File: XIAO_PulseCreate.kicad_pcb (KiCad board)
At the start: 2 copper layers, 72 x 48 mm, 19 parts, among them J1 MA735, J2 I2C OLED 0.91', J3 Power/Solenoid, J4 Trigger_IN, J5 Trigger_Out, Q1 2SK2232, SW1 MODE, SW2 +, SW3 -, U1 XIAO-RP2040-DIP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

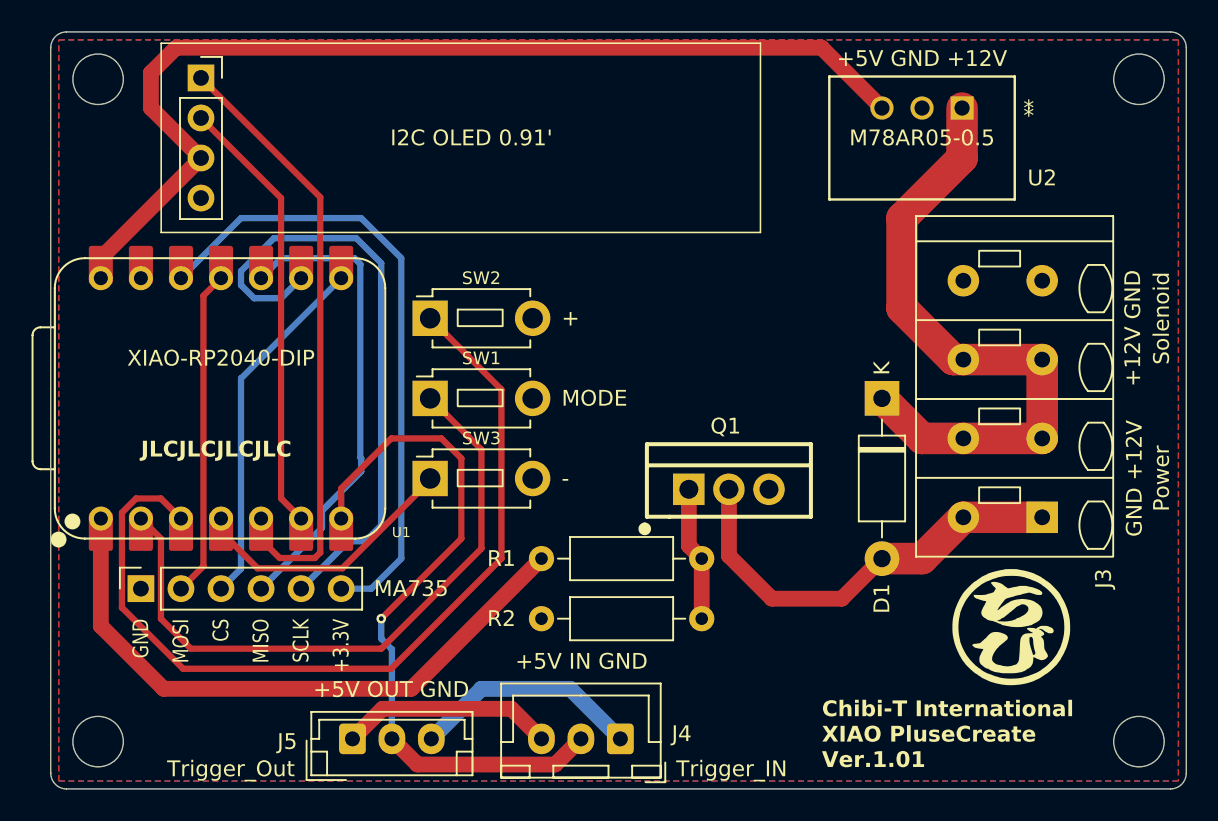
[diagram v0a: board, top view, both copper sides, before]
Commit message: Trigger_INの分圧抵抗を追加。 基板のソレノイドと電源の表記が逆だったので修正
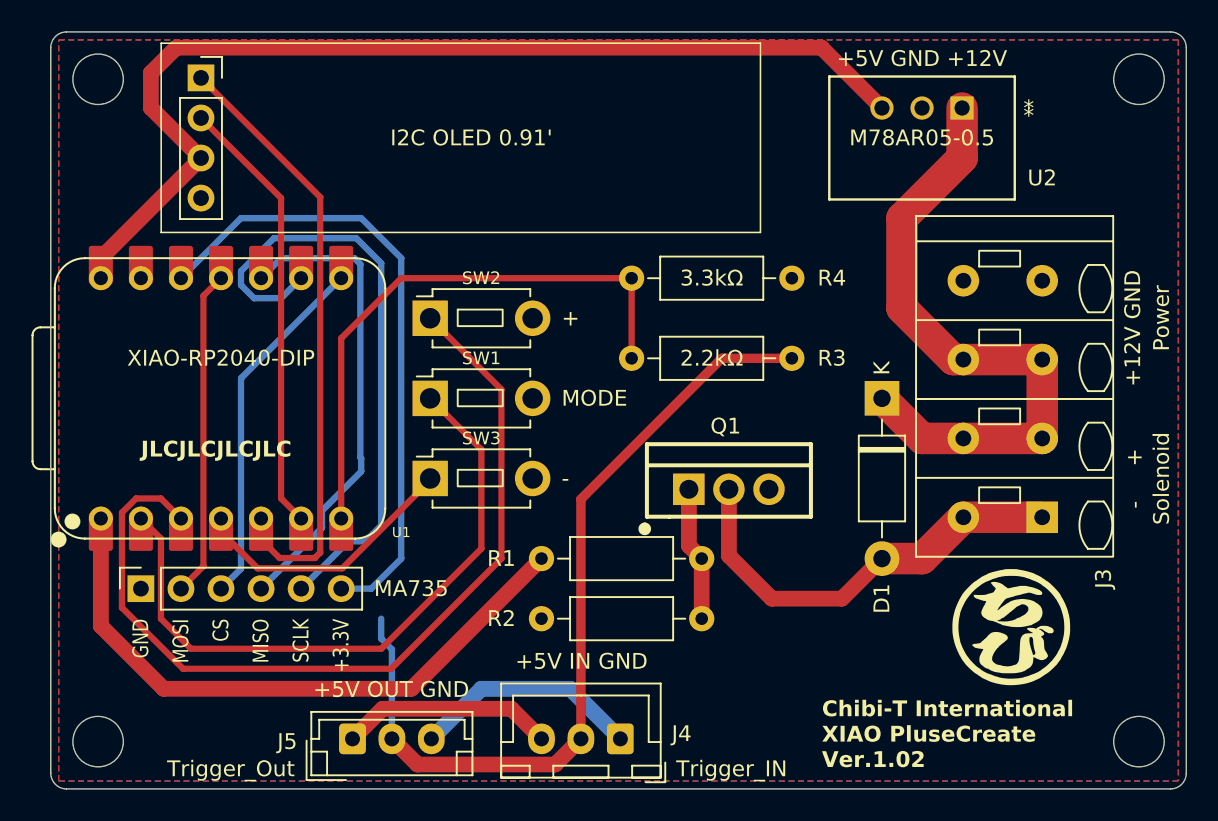
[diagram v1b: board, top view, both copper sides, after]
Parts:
- added R3: 2.2kΩ, Resistor_THT:R_Axial_DIN0207_L6.3mm_D2.5mm_P10.16mm_Horizontal, F.Cu at (177.0, 102.7)
- added R4: 3.3kΩ, Resistor_THT:R_Axial_DIN0207_L6.3mm_D2.5mm_P10.16mm_Horizontal, F.Cu at (177.0, 97.6)
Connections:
- net Net-(D1-A) renamed /-
- J4 pad 2: Trigger_IN -> Net-(J4-Pin_2)
- J5 pad 2: Trigger_IN -> Net-(J4-Pin_2)
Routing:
- net Net-(J4-Pin_2): track 0.00 -> 53.5 mm
- net Trigger_IN: track 44.9 -> 36.5 mm, vias 1 -> 0
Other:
- board text added: "- +"
- board text added: "Chibi-T International XIAO PluseCreate Ver.1.02"
- board text removed: "Chibi-T International XIAO PluseCreate Ver.1.01"
- board text removed: "GND +12V"

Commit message: MOSFETのヒートシンク取付を想定しレイアウト変更
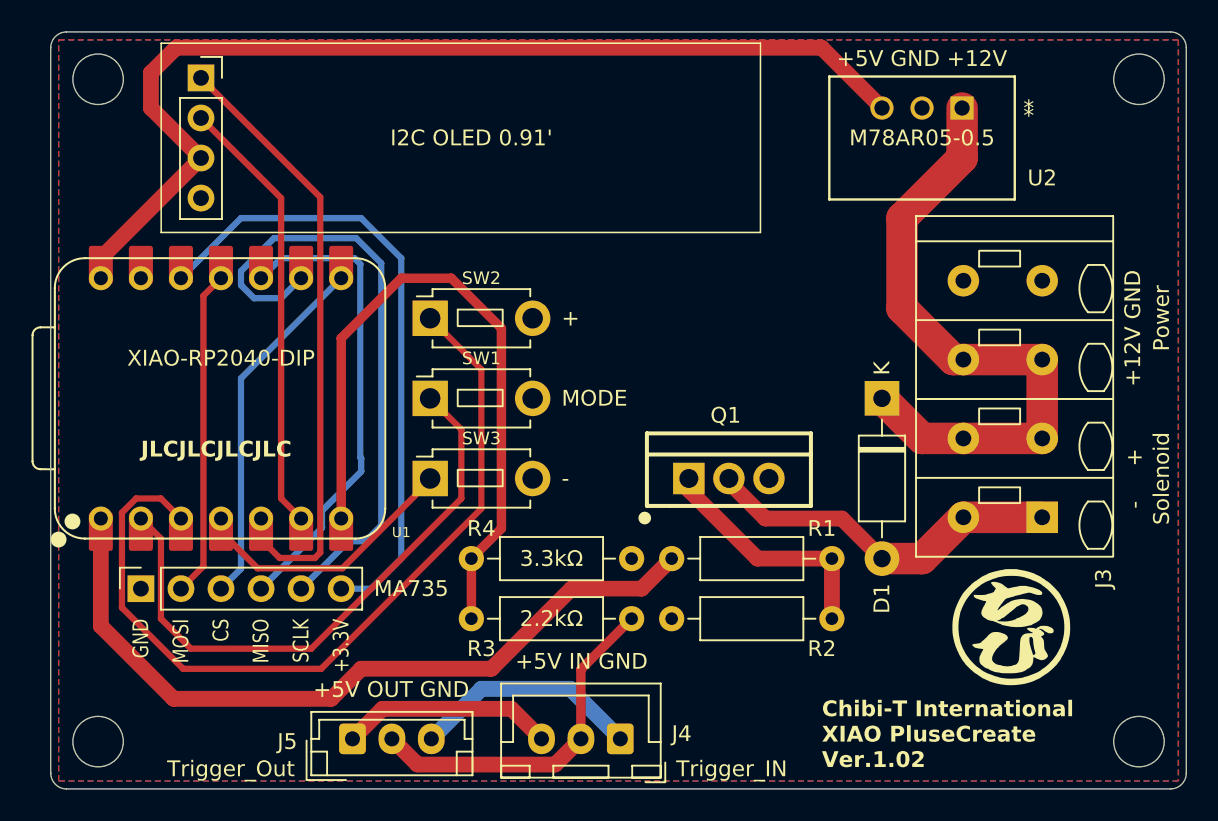
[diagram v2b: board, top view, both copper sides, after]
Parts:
- moved R4 20.5 mm to (166.8, 115.4)
- moved R3 19.4 mm to (166.8, 119.2)
- moved R1 8.25 mm to (169.4, 115.4)
- moved R2 8.25 mm to (169.4, 119.2)
- moved Q1 0.69 mm to (173.0, 110.3)
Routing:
- net Net-(J4-Pin_2): track 53.5 -> 22.3 mm
- net Pulse_Out: track 39.8 -> 48.6 mm
- net Trigger_IN: track 36.5 -> 43.7 mm
- net Net-(Q1-G): track 8.54 -> 15.4 mm
- net /-: track 27.3 -> 23.2 mm
- net ModeButton: track 41.5 -> 37.8 mm
- net +button: track 56.3 -> 52.7 mm

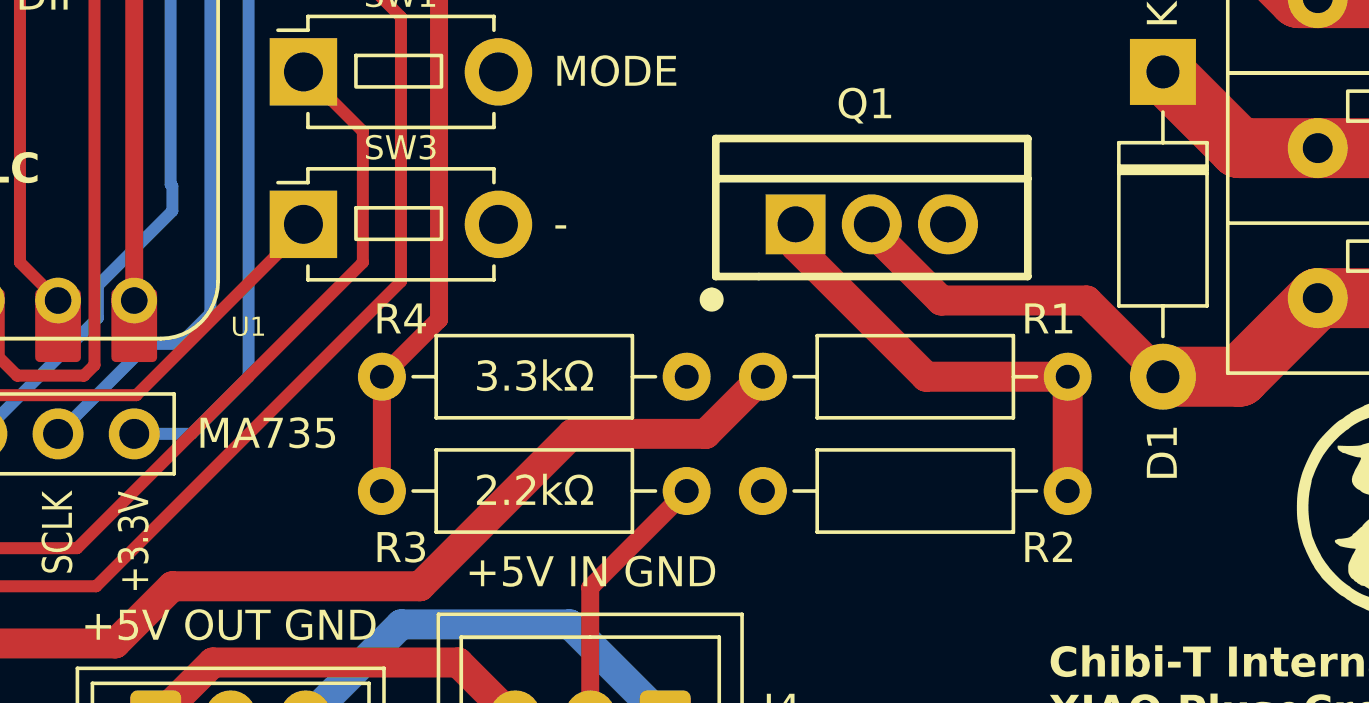
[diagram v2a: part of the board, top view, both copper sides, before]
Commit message: MOSFETをIRLZ34Nに変更
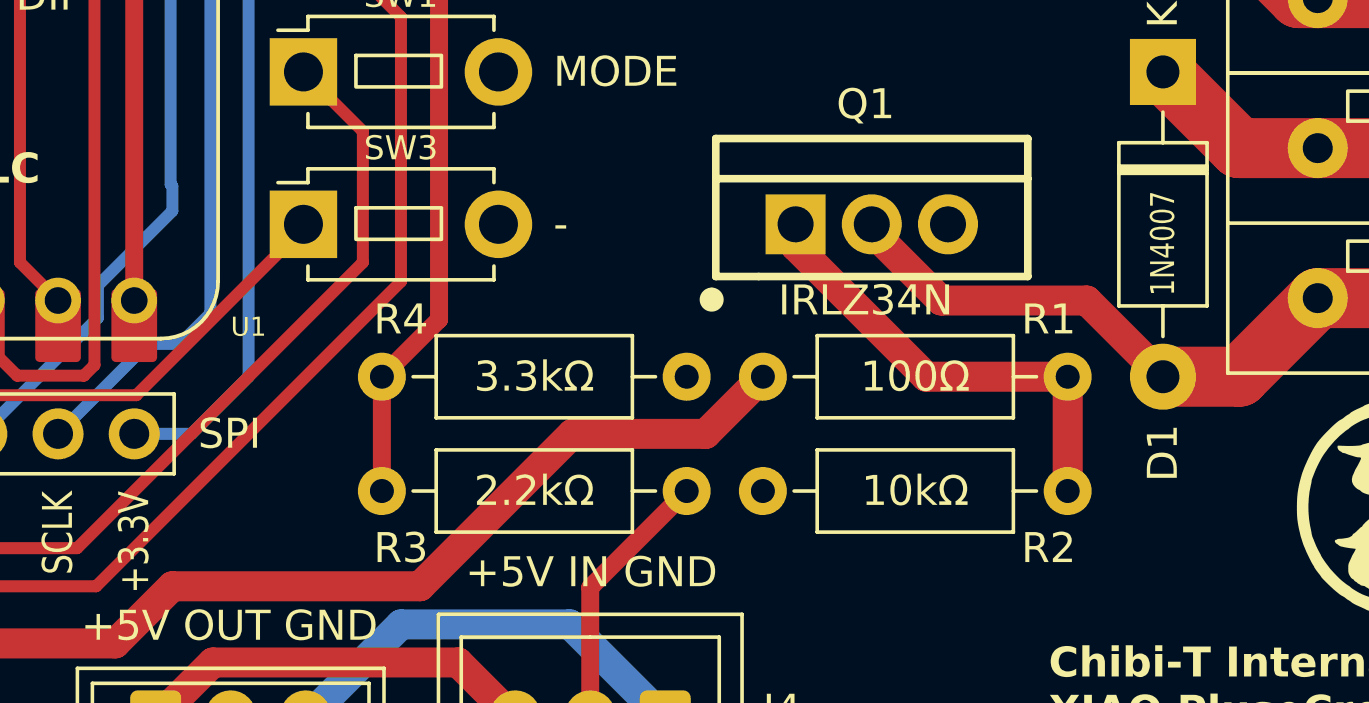
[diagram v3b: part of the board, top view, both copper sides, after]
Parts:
- J1: value MA735 -> SPI
- Q1: value 2SK2232 -> IRLZ34N
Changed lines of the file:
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@@
 	(title_block
 		(title "XIAO PluseCreate PCB")
-		(date "2025-02-11")
-		(rev "1.02")
+		(date "2025-02-19")
+		(rev "1.03")
 		(company "Chibi-T International")
 		(comment 1 "Tomohiro Kusu")
@@
 		)
 		(property "Value" "100Ω"
-			(at 5.08 2.37 0)
-			(layer "F.Fab")
-			(hide yes)
+			(at 5.08 0 0)
+			(layer "F.SilkS")
 			(effects
 				(font
@@
 		)
 		(property "Value" "1N4007"
-			(at 11.43 -2.54 90)
-			(layer "F.Fab")
+			(at 5.715 0 90)
+			(layer "F.SilkS")
 			(effects
 				(font
-					(size 1 1)
-					(thickness 0.15)
+					(size 0.8 0.65)
+					(thickness 0.1)
 				)
 			)
@@
 		)
 		(property "Value" "10kΩ"
-			(at 5.08 2.37 0)
-			(layer "F.Fab")
-			(hide yes)
+			(at 5.08 0 0)
+			(layer "F.SilkS")
 			(effects
 				(font
@@
 			)
 		)
-		(property "Value" "2SK2232"
+		(property "Value" "IRLZ34N"
 			(at -0.205258 2.54 0)
-			(layer "F.Fab")
+			(layer "F.SilkS")
 			(effects
 				(font
@@
 			)
 		)
-		(property "Value" "MA735"
-			(at 0 17.145 180)
+		(property "Value" "SPI"
+			(at 0 15.875 180)
 			(layer "F.SilkS")
 			(effects
